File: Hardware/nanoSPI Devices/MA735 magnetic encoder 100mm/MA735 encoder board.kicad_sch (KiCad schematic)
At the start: 4 parts, among them J1 FPC contacts 0.3mm, U1 MA735GGU-Z

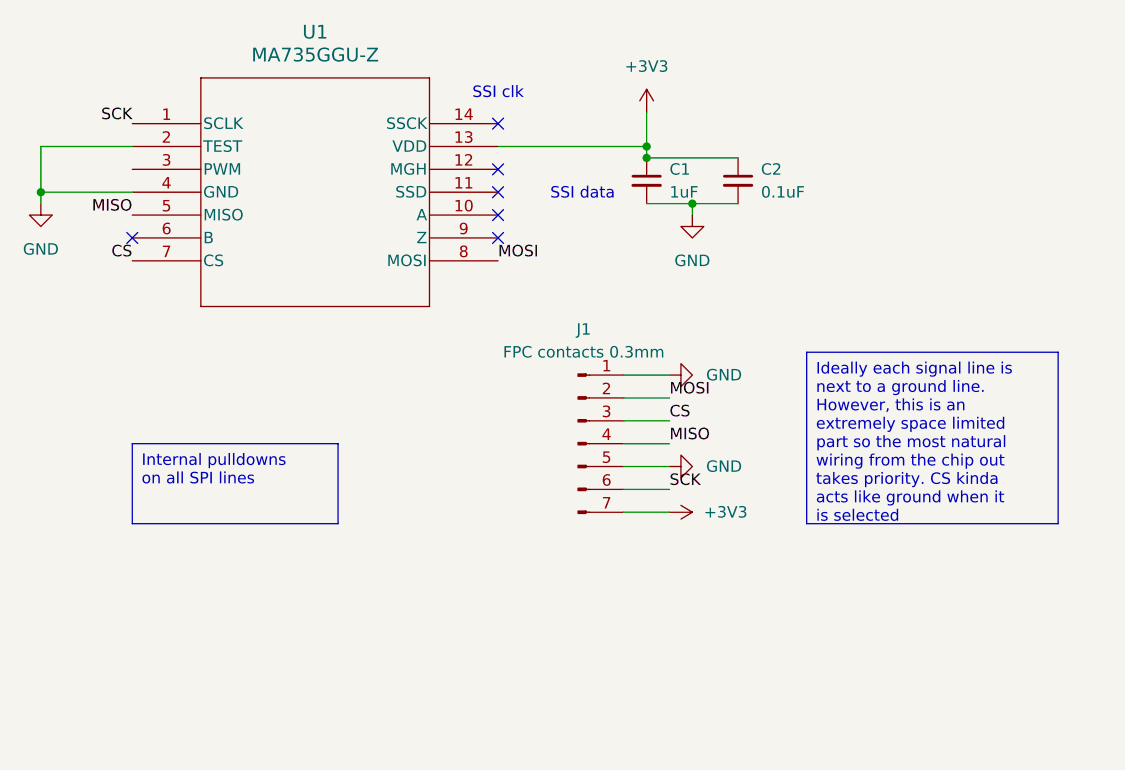
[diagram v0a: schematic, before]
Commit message: Exported Gerbers for MA735 encoder
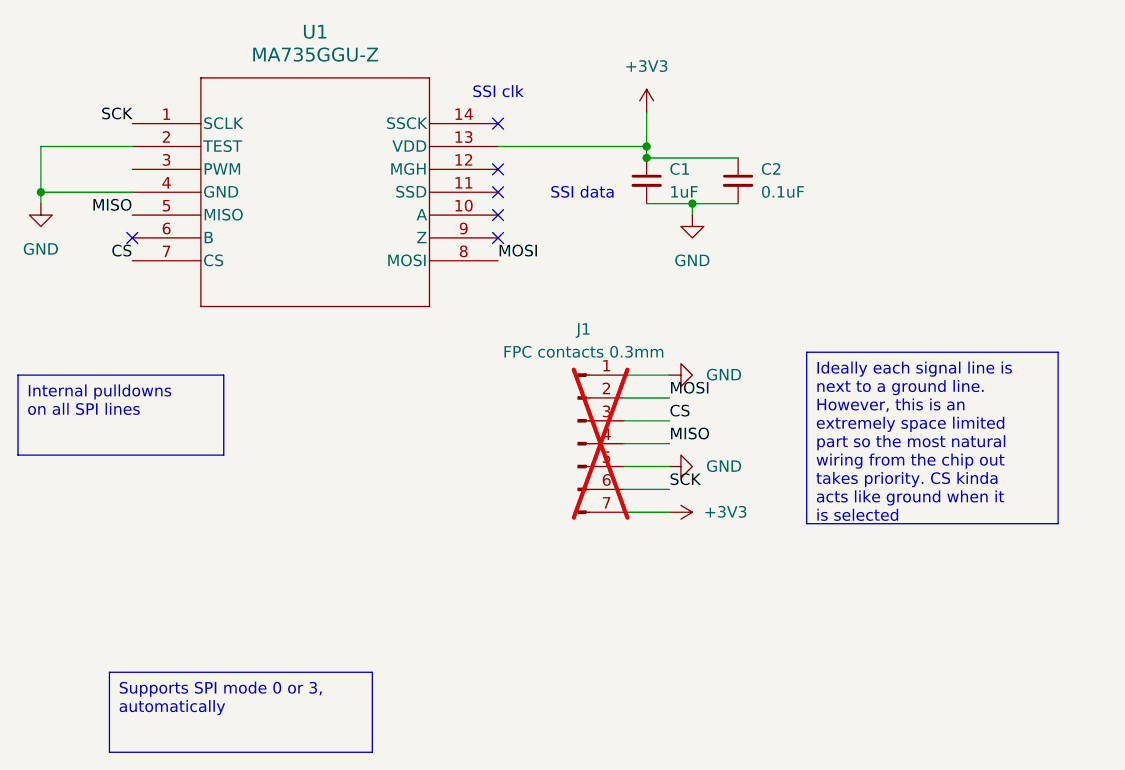
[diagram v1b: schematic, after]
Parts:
- C1: LCSC (none) -> C52923
- C2: LCSC (none) -> C1525
- J1: now not fitted
- U1: LCSC (none) -> C17233427
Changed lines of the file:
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@@
+		)
+	)
+	(text_box "Supports SPI mode 0 or 3, automatically"
+		(exclude_from_sim no)
+		(at 118.11 138.43 0)
+		(size 29.21 8.89)
+		(stroke
+			(width 0)
+			(type default)
+		)
+		(fill
+			(type none)
+		)
+		(effects
+			(font
+				(size 1.27 1.27)
+			)
+			(justify left top)
 		)
 	)
@@
 	(text_box "Internal pulldowns on all SPI lines"
 		(exclude_from_sim no)
-		(at 120.65 113.03 0)
+		(at 107.95 105.41 0)
 		(size 22.86 8.89)
 		(stroke
@@
 		(property "Description" "Unpolarized capacitor, small symbol"
 			(at 177.8 83.82 0)
+			(effects
+				(font
+					(size 1.27 1.27)
+				)
+				(hide yes)
+			)
+		)
+		(property "LCSC" "C52923"
+			(at 180.34 82.5562 0)
 			(effects
 				(font
@@
 			)
 		)
+		(property "LCSC" "C1525"
+			(at 190.5 82.5562 0)
+			(effects
+				(font
+					(size 1.27 1.27)
+				)
+				(hide yes)
+			)
+		)
 		(pin "1"
 		)
@@
 			)
 		)
+		(property "LCSC" "C17233427"
+			(at 140.97 67.31 0)
+			(effects
+				(font
+					(size 1.27 1.27)
+				)
+				(hide yes)
+			)
+		)
 		(pin "6"
 		)
@@
 		(in_bom yes)
 		(on_board yes)
-		(dnp no)
+		(dnp yes)
 		(fields_autoplaced yes)
 		(property "Reference" "J1"
